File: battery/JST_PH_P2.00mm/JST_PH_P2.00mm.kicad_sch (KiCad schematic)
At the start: 1 part

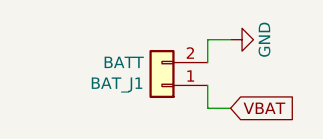
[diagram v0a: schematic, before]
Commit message: update power switch
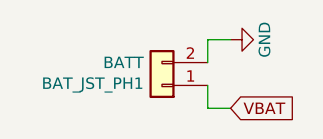
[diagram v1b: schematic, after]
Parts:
- renumbered BAT_J1 to BAT_JST_PH1
